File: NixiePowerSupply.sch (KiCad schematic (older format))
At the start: 18 parts

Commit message: Base schematics comp
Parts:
- removed C?: 100uF, symbol C
- added C1: 100uF_16V, Capacitors_THT:CP_Radial_D5.0mm_P2.00mm, symbol CP
- added J1: BARREL_JACK, Connectors:BARREL_JACK, symbol BARREL_JACK
- added J2: CONN_01X04, Pin_Headers:Pin_Header_Straight_1x04_Pitch2.54mm, symbol CONN_01X04
- added J3: CONN_01X05, Pin_Headers:Pin_Header_Straight_1x05_Pitch2.54mm, symbol CONN_01X05
- added U2: 7805, TO_SOT_Packages_THT:TO-220-3_Vertical, symbol 7805
- C2, C4: renamed from C?; footprint (none) -> Capacitors_THT:C_Disc_D5.0mm_W2.5mm_P2.50mm
- C3: renamed from C?; footprint (none) -> Capacitors_THT:C_Disc_D5.0mm_W2.5mm_P5.00mm
- C5: renamed from C?; value 4.7u -> 4.7u_400V; footprint (none) -> Capacitors_THT:CP_Radial_D10.0mm_P5.00mm
- D1: renamed from D?; footprint (none) -> Diodes_THT:D_DO-15_P5.08mm_Vertical_AnodeUp
- D2: renamed from 1N4148; value D -> 1N4148; footprint (none) -> Diodes_THT:D_DO-35_SOD27_P7.62mm_Horizontal
- L1: renamed from 470uH; value L -> 470uH; footprint (none) -> NixiePowerSupply:Inductors_LHL13NB471K
- Q1: renamed from Q?; footprint (none) -> TO_SOT_Packages_THT:TO-92_Inline_Narrow_Oval
- Q2: renamed from Q?; footprint (none) -> TO_SOT_Packages_THT:TO-220-3_Vertical
- R1: renamed from R?; footprint (none) -> Resistors_THT:R_Axial_DIN0309_L9.0mm_D3.2mm_P12.70mm_Horizontal
- R2, R3, R4, R6: renamed from R?; footprint (none) -> Resistors_THT:R_Axial_DIN0207_L6.3mm_D2.5mm_P10.16mm_Horizontal
- R5: renamed from R?; footprint (none) -> NixiePowerSupply:VOL_3362P-1-202LF
- R7: renamed from 0.15; value R -> 0.15; footprint (none) -> Resistors_THT:R_Axial_DIN0414_L11.9mm_D4.5mm_P15.24mm_Horizontal
- U1: renamed from U?; footprint (none) -> Housings_DIP:DIP-8_W7.62mm
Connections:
- net +12V: now also C1.1, J1.1, U2.VI
- net +HV: now also J3.1 (P1), J3.2 (P2)
- net GND: now also C1.2, J1.2, J1.3, J2.4 (P4), J3.4 (P4), J3.5 (P5), U2.GND
- new net +5V: J2.1 (P1), U2.VO
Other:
- moved on the sheet: C2, C3, C4, C5, D1, D2, L1, Q1, Q2, R1, R2, R3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

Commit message: Modify cap footprint
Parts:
- C1: footprint Capacitors_THT:CP_Radial_D5.0mm_P2.00mm -> Capacitors_THT:CP_Radial_D6.3mm_P2.50mm
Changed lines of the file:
@@
 F 0 "C1" H 2725 4150 50  0000 L CNN
 F 1 "100uF_16V" H 2250 3950 50  0000 L CNN
-F 2 "Capacitors_THT:CP_Radial_D5.0mm_P2.00mm" H 2738 3900 50  0001 C CNN
+F 2 "Capacitors_THT:CP_Radial_D6.3mm_P2.50mm" H 2738 3900 50  0001 C CNN
 F 3 "" H 2700 4050 50  0001 C CNN
 	1    2700 4050

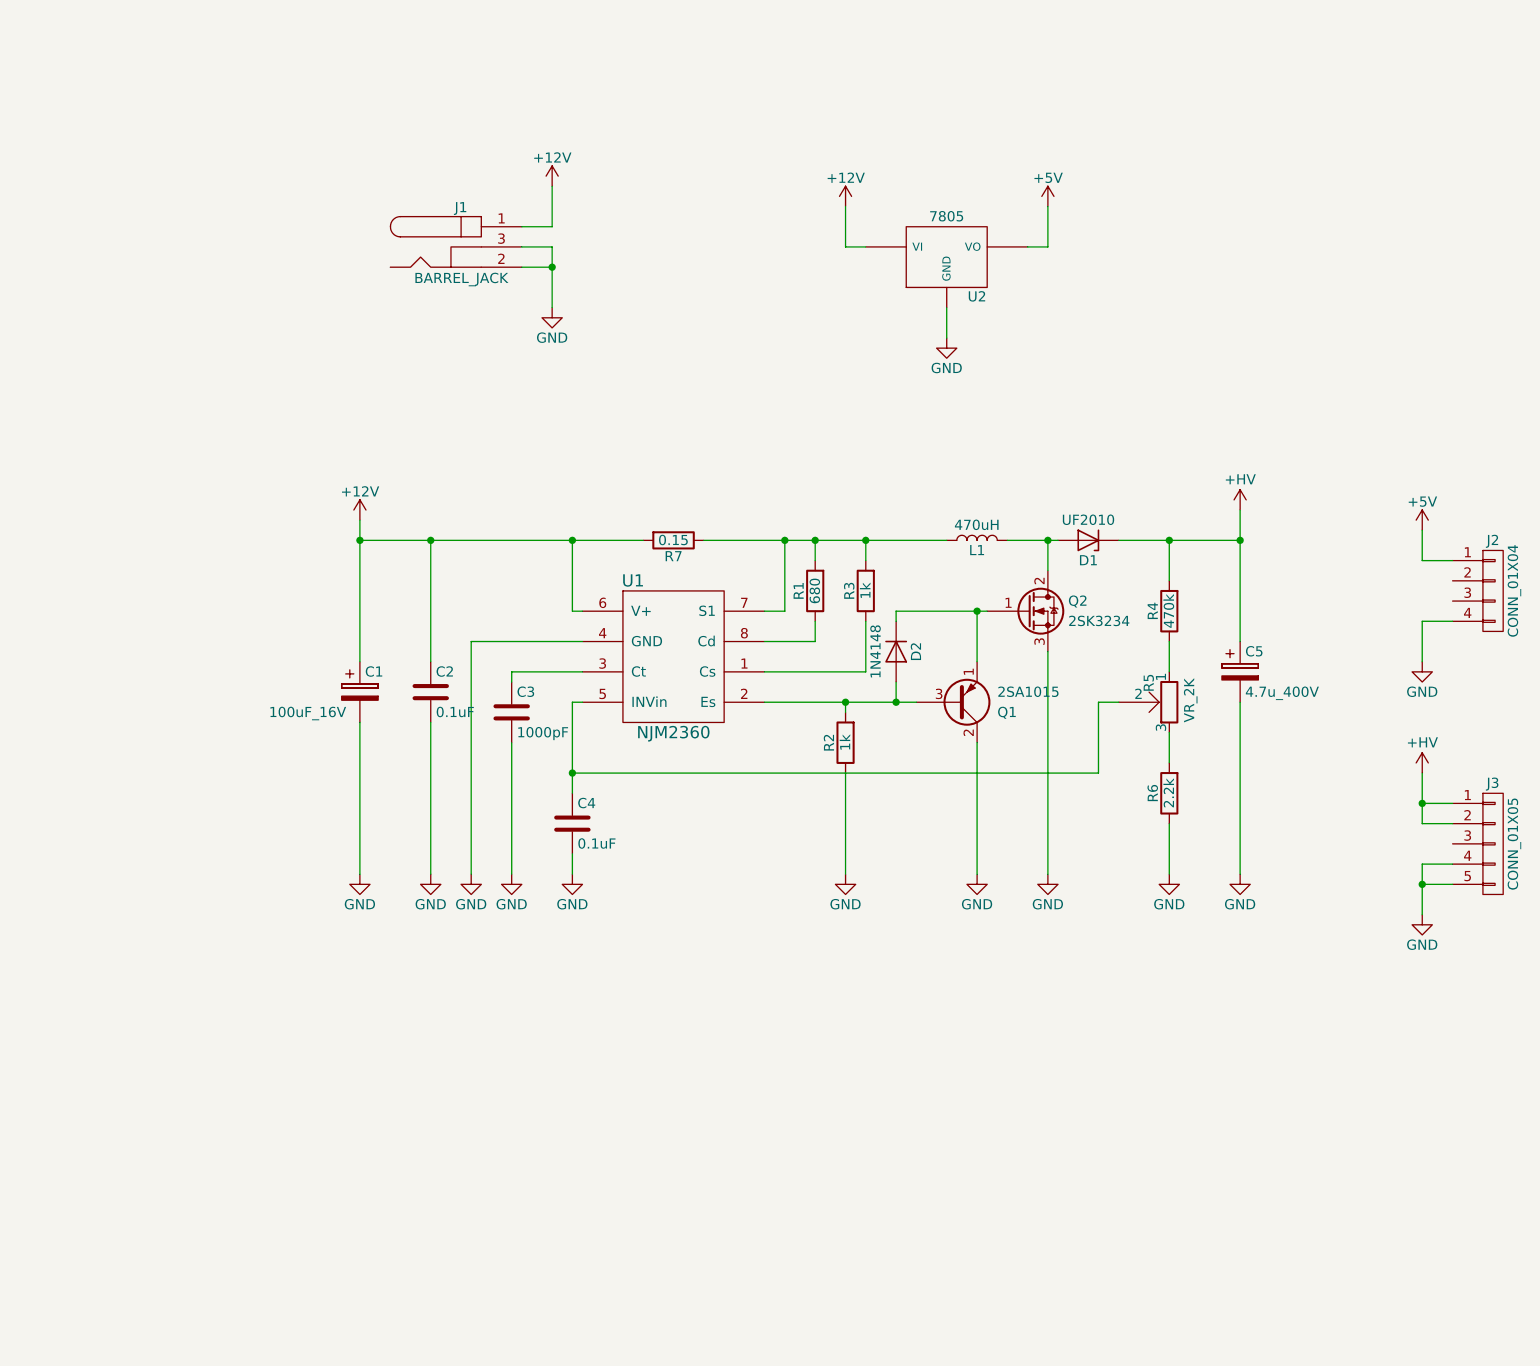
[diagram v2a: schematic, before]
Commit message: parts moved for layout chnge
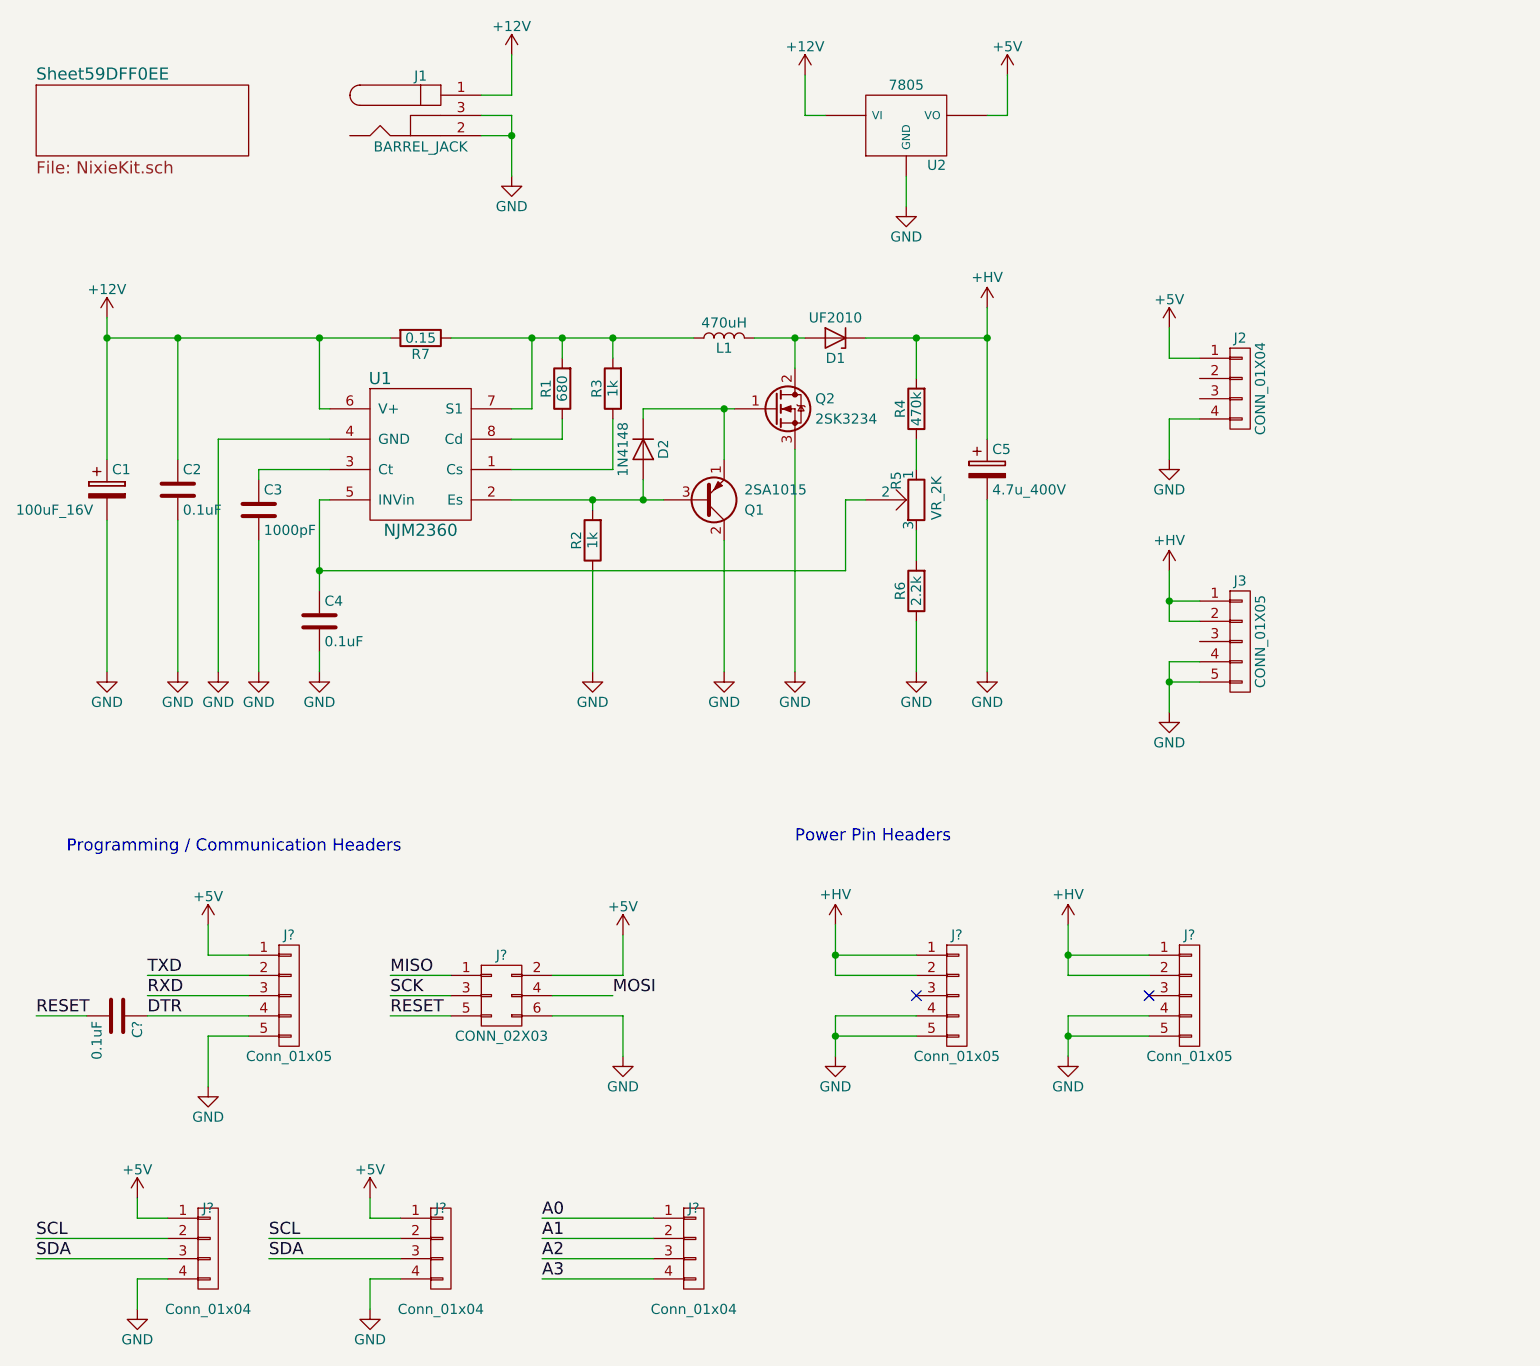
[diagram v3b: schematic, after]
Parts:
- added C?: 0.1uF, Capacitors_THT:C_Disc_D5.0mm_W2.5mm_P2.50mm, symbol C
- added J? (x3): Conn_01x05, Pin_Headers:Pin_Header_Straight_1x05_Pitch2.54mm, symbol CONN_01X05
- added J? (x3): Conn_01x04, Pin_Headers:Pin_Header_Straight_1x04_Pitch2.54mm, symbol CONN_01X04
- added J?: CONN_02X03, symbol CONN_02X03
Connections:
- net +5V: now also J?.1 (P1), J?.1 (P1), J?.1 (P1), J?.2 (P2)
- net +HV: now also J?.1 (P1), J?.1 (P1), J?.2 (P2), J?.2 (P2)
- net GND: now also J?.4 (P4), J?.4 (P4), J?.4 (P4), J?.4 (P4), J?.5 (P5), J?.5 (P5), J?.5 (P5), J?.6 (P6)
- new net A0: J?.1 (P1)
- new net A1: J?.2 (P2)
- new net A2: J?.3 (P3)
- new net A3: J?.4 (P4)
- new net DTR: C?.1, J?.4 (P4)
- new net MISO: J?.1 (P1)
- new net MOSI: J?.4 (P4)
- new net RESET: C?.2, J?.5 (P5)
- new net RXD: J?.3 (P3)
- new net SCK: J?.3 (P3)
- new net SCL: J?.2 (P2), J?.2 (P2)
- new net SDA: J?.3 (P3), J?.3 (P3)
- new net TXD: J?.2 (P2)
- no-connect marks 0 -> 2
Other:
- note added: "Power Pin Headers"
- note added: "Programming / Communication Headers"
- moved on the sheet: C1, C2, C3, C4, C5, D1, D2, J1, J2, J3, L1, Q1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
